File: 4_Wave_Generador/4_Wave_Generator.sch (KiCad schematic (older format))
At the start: 119 parts, among them J1 RS232, J10 Jumper, J11 Jumper, J12 Jumper, J13 Jumper, J14 Jumper, J15 Jumper, J2 I2C, J3 RS232_PIC, J4 RESET, J5 Jumper, J7 Jumper, P1 ECG INPUTS, P10 INPUT_ADC_PIC, P11 PWM_MUX1, P12 RG_8421, P13 CON_MUX2, P14 OUTPUT_TARJET, P15 OUTPUT_DIG_PIC, P16 OUTPUT_DIG_ATMEGA328P, P2 PIC_PROGRAMER, P3 SPI, P4 AD8232_CONTROL, P5 ENTRADA_OXIMETRO, P6 CONN_01X04, P7 CONN_01X04, P8 MCLK_EXTERNAL, P9 SPI_AD9833, SW1 SW_Push, SW2 RESET_PIC, U1 PIC16F688, U2 AD8232_A, U3 ATMEGA328P-AU_MIO, U4 AD9833, U5 LD1117S33TR_MIO, U6 ADG819, U7 ADG819, U8 AD8421, Y1 Crystal_8MHz, Y2 XRCHA_16M

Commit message: GENERADOR_V8
ORGANIZACION DE ELEMENTOS
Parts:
- removed P5: ENTRADA_OXIMETRO, symbol CONN_02X03
- removed R17: 1K, Resistors_SMD:R_0805_HandSoldering, symbol 1K
- added JP5: PASO_A/D, Pin_Headers:Pin_Header_Straight_1x02_Pitch2.54mm, symbol PASO_A/D
- added P5: OXIMETRO, Foot_Prints_Manager_Outputs:OXIMETRO, symbol CONN_01X03
- added P?: 5V, Foot_Prints_Manager_Outputs:SUPPLY_5V, symbol CONN_01X04
- added R17: 20K, Resistors_SMD:R_0805_HandSoldering, symbol 20K
- JP4: value AREF -> J_AREF
- P10: footprint (none) -> Foot_Prints_Manager_Outputs:ADC_PIC
- P11: value PWM_MUX1 -> IN_MUX1; footprint (none) -> Foot_Prints_Manager_Outputs:IN_MUX1
- P12: footprint (none) -> Foot_Prints_Manager_Outputs:RG_8421
- P13: value CON_MUX2 -> IN_MUX2; footprint (none) -> Foot_Prints_Manager_Outputs:IN_MUX2
- P14: footprint (none) -> Foot_Prints_Manager_Outputs:VOUT
- P15: footprint (none) -> Pin_Headers:Pin_Header_Straight_1x04_Pitch2.54mm
- P16: footprint (none) -> Foot_Prints_Manager_Outputs:OUTPUT_ATMEGA
- P2: footprint Pin_Headers:Pin_Header_Angled_1x05_Pitch2.54mm -> Foot_Prints_Manager_Outputs:PIC_PROGRAMER
- P3: value SPI -> SPI_MICRO
- P6: value CONN_01X04 -> SUPPLY -12; footprint Pin_Headers:Pin_Header_Angled_1x04_Pitch2.54mm -> Foot_Prints_Manager_Outputs:SUPPLY_-12V
- P7: value CONN_01X04 -> SUPPLY +12; footprint Pin_Headers:Pin_Header_Angled_1x04_Pitch2.54mm -> Foot_Prints_Manager_Outputs:SUPPLY_12V
- P8: footprint Pin_Headers:Pin_Header_Angled_1x04_Pitch2.54mm -> Foot_Prints_Manager_Outputs:MCLK_EXTERNAL
- P9: footprint (none) -> Foot_Prints_Manager_Outputs:SPI_AD9833
- W1, W10, W11, W12, W2, W3, W4, W5, W6, W7, W8, W9: footprint (none) -> Measurement_Points:Measurement_Point_Round-TH_Small
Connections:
- net labels added: OXIMETRO, RG_PIN2, RG_PIN3
- net labels removed: A_AD5270_1, OXI_1, OXI_2, OXI_3, W_AD5270_1
- wire segments 343 -> 345
- no-connect marks 6 -> 8
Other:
- note added: "MICROCONTROLLER \nATMEGA 328P"
- note removed: "MICROCONTROLADOR \nATMEGA 328P"
- moved on the sheet: C10, D1, D3, D5, D7, P6, P7, R2, R22, R23, R24

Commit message: GENERADOR_V9
DISTRIBUCION DE COMPONENTES
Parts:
- removed C13: 0.1uF, Capacitors_SMD:C_0805_HandSoldering, symbol 0.1uF
- removed J1: RS232, Foot_Prints_Manager_Outputs:RS232, symbol CONN_01X03
- removed J2: I2C, Foot_Prints_Manager_Outputs:I2C_2X4, symbol CONN_01X02
- removed J3: RS232_PIC, Foot_Prints_Manager_Outputs:RS232, symbol CONN_01X03
- removed P11: IN_MUX1, Foot_Prints_Manager_Outputs:IN_MUX1, symbol CONN_01X02
- removed P15: OUTPUT_DIG_PIC, Pin_Headers:Pin_Header_Straight_1x04_Pitch2.54mm, symbol CONN_01X04
- removed P16: OUTPUT_DIG_ATMEGA328P, Foot_Prints_Manager_Outputs:OUTPUT_ATMEGA, symbol CONN_01X12
- removed P6: SUPPLY -12, Foot_Prints_Manager_Outputs:SUPPLY_-12V, symbol CONN_01X04
- removed P7: SUPPLY +12, Foot_Prints_Manager_Outputs:SUPPLY_12V, symbol CONN_01X04
- removed P?: 5V, Foot_Prints_Manager_Outputs:SUPPLY_5V, symbol CONN_01X04
- added C9: 0.1uF, Capacitors_SMD:C_0805_HandSoldering, symbol 0.1uF
- added J6, J8: Jumper, Pin_Headers:Pin_Header_Straight_1x02_Pitch2.54mm, symbol Jumper-RESCUE-PCB_OSCILLATOR
- added JP6: MIN_SANGRADO, Pin_Headers:Pin_Header_Straight_1x03_Pitch2.54mm, symbol JUMPER3
- added P15: MUX_S1, Pin_Headers:Pin_Header_Straight_1x02_Pitch2.54mm, symbol CONN_01X02
- added P16: PD5, Pin_Headers:Pin_Header_Straight_1x01_Pitch2.54mm, symbol CONN_01X01
- added P17: SUPPLY_-12V, Foot_Prints_Manager_Outputs:SUPPLY_-12V, symbol CONN_01X02
- added P18: RS232, Foot_Prints_Manager_Outputs:RS232, symbol CONN_01X03
- added P19: I2C, Foot_Prints_Manager_Outputs:I2C_2X4, symbol CONN_01X02
- added P20: PD6, Pin_Headers:Pin_Header_Straight_1x01_Pitch2.54mm, symbol CONN_01X01
- added P21: PD7, Pin_Headers:Pin_Header_Straight_1x01_Pitch2.54mm, symbol CONN_01X01
- added P22: PB0, Pin_Headers:Pin_Header_Straight_1x01_Pitch2.54mm, symbol CONN_01X01
- added P23: PB1, Pin_Headers:Pin_Header_Straight_1x01_Pitch2.54mm, symbol CONN_01X01
- added P24: PC0, Pin_Headers:Pin_Header_Straight_1x01_Pitch2.54mm, symbol CONN_01X01
- added P25: PC1, Pin_Headers:Pin_Header_Straight_1x01_Pitch2.54mm, symbol CONN_01X01
- added P26: PC2, Pin_Headers:Pin_Header_Straight_1x01_Pitch2.54mm, symbol CONN_01X01
- added P27: PC3, Pin_Headers:Pin_Header_Straight_1x01_Pitch2.54mm, symbol CONN_01X01
- added P28: PD2, Pin_Headers:Pin_Header_Straight_1x01_Pitch2.54mm, symbol CONN_01X01
- added P29: PD3, Pin_Headers:Pin_Header_Straight_1x01_Pitch2.54mm, symbol CONN_01X01
- added P30: PD4, Pin_Headers:Pin_Header_Straight_1x01_Pitch2.54mm, symbol CONN_01X01
- added P31, P32, P33, P34: TORNILLO, Mounting_Holes:MountingHole_3.2mm_M3_Pad_Via, symbol CONN_01X01
- added P35: RS232_PIC, Foot_Prints_Manager_Outputs:RS232, symbol CONN_01X03
- added P6: SUPPLY_12V, Foot_Prints_Manager_Outputs:SUPPLY_12V, symbol CONN_01X02
- added P7: SUPPLY_VDD, Foot_Prints_Manager_Outputs:SUPPLY_5V, symbol CONN_01X02
- added U9: ADG819, Housings_SSOP:MSOP-8_3x3mm_Pitch0.65mm, symbol ADG819
- P13: value IN_MUX2 -> OUTPUT_DIG_PIC; footprint Foot_Prints_Manager_Outputs:IN_MUX2 -> Pin_Headers:Pin_Header_Straight_1x02_Pitch2.54mm
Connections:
- net labels added: MODULATED, PWM, PWM_ATMEGA, SELECTOR
- net labels removed: PD5, PD6, PD7, SDN_OFF
- no-connect marks 8 -> 15
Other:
- note added: "MULTIPLEXER_3\n"
- note removed: "MUX_1\n"
- note removed: "MUX_2"
- moved on the sheet: C14, C15, C16, C17, C20, C21, C22, C23, C24, C25, C26, C28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

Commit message: GENERADOR_V10
RUTEADO MICRO
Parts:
- removed P16: PD5, Pin_Headers:Pin_Header_Straight_1x01_Pitch2.54mm, symbol CONN_01X01
- removed P20: PD6, Pin_Headers:Pin_Header_Straight_1x01_Pitch2.54mm, symbol CONN_01X01
- removed P21: PD7, Pin_Headers:Pin_Header_Straight_1x01_Pitch2.54mm, symbol CONN_01X01
- removed P22: PB0, Pin_Headers:Pin_Header_Straight_1x01_Pitch2.54mm, symbol CONN_01X01
- removed P23: PB1, Pin_Headers:Pin_Header_Straight_1x01_Pitch2.54mm, symbol CONN_01X01
- removed P24: PC0, Pin_Headers:Pin_Header_Straight_1x01_Pitch2.54mm, symbol CONN_01X01
- removed P25: PC1, Pin_Headers:Pin_Header_Straight_1x01_Pitch2.54mm, symbol CONN_01X01
- removed P26: PC2, Pin_Headers:Pin_Header_Straight_1x01_Pitch2.54mm, symbol CONN_01X01
- removed P27: PC3, Pin_Headers:Pin_Header_Straight_1x01_Pitch2.54mm, symbol CONN_01X01
- removed P28: PD2, Pin_Headers:Pin_Header_Straight_1x01_Pitch2.54mm, symbol CONN_01X01
- removed P29: PD3, Pin_Headers:Pin_Header_Straight_1x01_Pitch2.54mm, symbol CONN_01X01
- removed P30: PD4, Pin_Headers:Pin_Header_Straight_1x01_Pitch2.54mm, symbol CONN_01X01
- added P11: DIG_ATMEGA, Pin_Headers:Pin_Header_Straight_1x04_Pitch2.54mm, symbol CONN_01X04
- added P16: DIG_MICRO, Pin_Headers:Pin_Header_Straight_1x03_Pitch2.54mm, symbol CONN_01X03
- added P20: DIG_ATMEGA2, Pin_Headers:Pin_Header_Straight_1x03_Pitch2.54mm, symbol CONN_01X03
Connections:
- net MODULATING_WAVE is gone; now on net SELECTOR: U3.10 ((PCINT22/OC0A/AIN0)PD6)
- net PB0: now also P20.2 (P2)
- net PB1: now also P20.3 (P3)
- net PC0: now also P11.1 (P1)
- net PC1: now also P11.2 (P2)
- net PC2: now also P11.3 (P3)
- net PC3: now also P11.4 (P4)
- net PD2: now also P16.1 (P1)
- net PD3: now also P16.2 (P2)
- net PD4: now also P16.3 (P3)
- net SELECTOR: no longer U3.11 ((PCINT23/AIN1)PD7)
- new net PD7: P20.1 (P1), U3.11 ((PCINT23/AIN1)PD7)
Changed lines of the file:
@@
 Text Label 6170 2350 0    60   ~ 0
 PD3
-Text Label 8090 10870 1    60   ~ 0
+Text Label 8260 10860 1    60   ~ 0
 PC3
-Text Label 7790 10870 1    60   ~ 0
+Text Label 7960 10860 1    60   ~ 0
 PC0
-Text Label 7890 10870 1    60   ~ 0
+Text Label 8060 10860 1    60   ~ 0
 PC1
-Text Label 7990 10870 1    60   ~ 0
+Text Label 8160 10860 1    60   ~ 0
 PC2
-Text Label 7490 10870 1    60   ~ 0
-SELECTOR
 Text Notes 6010 1080 0    60   ~ 0
 MICROCONTROLLER \nATMEGA 328P
-Text Label 8290 10870 1    60   ~ 0
+Text Label 7150 10850 1    60   ~ 0
 PD3
-Text Label 8190 10870 1    60   ~ 0
+Text Label 7050 10850 1    60   ~ 0
 PD2
 Text Label 5610 2090 0    60   ~ 0
@@
 	7690 10100 7690 10870
 Wire Wire Line
-	7790 10100 7790 10870
-Wire Wire Line
-	7890 10100 7890 10870
-Wire Wire Line
-	7990 10100 7990 10870
-Wire Wire Line
-	7290 10100 7290 10870
-Wire Wire Line
-	7390 10100 7390 10870
+	7960 10090 7960 10860
+Wire Wire Line
+	8060 10090 8060 10860
+Wire Wire Line
+	8160 10090 8160 10860
 Wire Wire Line
 	7490 10100 7490 10870
@@
 	7590 10100 7590 10870
 Wire Wire Line
-	8090 10100 8090 10870
-Wire Wire Line
-	8290 10100 8290 10870
-Wire Wire Line
-	8390 10100 8390 10870
+	8260 10090 8260 10860
+Wire Wire Line
+	7150 10080 7150 10850
+Wire Wire Line
+	7250 10080 7250 10850
 Wire Notes Line
 	640  7890 4960 7890
@@
 OUTPUT GAVE GENERATOR
 Wire Wire Line
-	8190 10100 8190 10870
-Text Label 8390 10870 1    60   ~ 0
+	7050 10080 7050 10850
+Text Label 7250 10850 1    60   ~ 0
 PD4
 Text Label 6650 10870 1    60   ~ 0
@@
 P 6700 9900
 F 0 "P13" H 6700 10050 50  0000 C CNN
-F 1 "OUTPUT_DIG_PIC" V 6810 9830 50  0000 C CNN
+F 1 "OUTPUT_DIG_PIC" V 6820 9900 50  0000 C CNN
 F 2 "Pin_Headers:Pin_Header_Straight_1x02_Pitch2.54mm" H 6700 9900 50  0001 C CNN
 F 3 "" H 6700 9900 50  0000 C CNN
@@
 	0    -1   -1   0
 $EndComp
-Text Label 7390 10870 1    60   ~ 0
-MODULATING_WAVE
 Text Label 13340 5850 0    60   ~ 0
 BASE_WAVE
@@
 Text Label 11130 9130 0    60   ~ 0
 PWM_ATMEGA
-Text Label 7290 10870 1    60   ~ 0
-PWM_ATMEGA
 Wire Notes Line
 	9740 9500 9740 7920
@@
 Wire Notes Line
 	12740 7920 12740 9500
+Text Label 9240 1790 2    60   ~ 0
+PD7
 Text Label 9240 1700 2    60   ~ 0
-MODULATING_WAVE
-Text Label 9240 1790 2    60   ~ 0
 SELECTOR
 $Comp
@@
 	0    -1   -1   0
 $EndComp
-$Comp
-L CONN_01X01 P20
-U 1 1 59D7476C
-P 7390 9900
-F 0 "P20" V 7310 9910 50  0000 C CNN
-F 1 "PD6" H 7510 9900 50  0000 C CNN
-F 2 "Pin_Headers:Pin_Header_Straight_1x01_Pitch2.54mm" H 7390 9900 50  0001 C CNN
-F 3 "" H 7390 9900 50  0000 C CNN
-	1    7390 9900
-	0    -1   -1   0
-$EndComp
-$Comp
-L CONN_01X01 P21
-U 1 1 59D74A09
-P 7490 9900
-F 0 "P21" V 7410 9910 50  0000 C CNN
-F 1 "PD7" H 7610 9900 50  0000 C CNN
-F 2 "Pin_Headers:Pin_Header_Straight_1x01_Pitch2.54mm" H 7490 9900 50  0001 C CNN
-F 3 "" H 7490 9900 50  0000 C CNN
-	1    7490 9900
-	0    -1   -1   0
-$EndComp
-$Comp
-L CONN_01X01 P22
-U 1 1 59D7CC91
-P 7590 9900
-F 0 "P22" V 7510 9910 50  0000 C CNN
-F 1 "PB0" H 7710 9900 50  0000 C CNN
-F 2 "Pin_Headers:Pin_Header_Straight_1x01_Pitch2.54mm" H 7590 9900 50  0001 C CNN
-F 3 "" H 7590 9900 50  0000 C CNN
-	1    7590 9900
-	0    -1   -1   0
-$EndComp
-$Comp
-L CONN_01X01 P23
-U 1 1 59D7CC97
-P 7690 9900
-F 0 "P23" V 7610 9910 50  0000 C CNN
-F 1 "PB1" H 7810 9900 50  0000 C CNN
-F 2 "Pin_Headers:Pin_Header_Straight_1x01_Pitch2.54mm" H 7690 9900 50  0001 C CNN
-F 3 "" H 7690 9900 50  0000 C CNN
-	1    7690 9900
-	0    -1   -1   0
-$EndComp
-$Comp
-L CONN_01X01 P24
-U 1 1 59D7CC9D
-P 7790 9900
-F 0 "P24" V 7710 9910 50  0000 C CNN
-F 1 "PC0" H 7910 9900 50  0000 C CNN
-F 2 "Pin_Headers:Pin_Header_Straight_1x01_Pitch2.54mm" H 7790 9900 50  0001 C CNN
-F 3 "" H 7790 9900 50  0000 C CNN
-	1    7790 9900
-	0    -1   -1   0
-$EndComp
-$Comp
-L CONN_01X01 P25
-U 1 1 59D88535
-P 7890 9900
-F 0 "P25" V 7810 9910 50  0000 C CNN
-F 1 "PC1" H 8010 9900 50  0000 C CNN
-F 2 "Pin_Headers:Pin_Header_Straight_1x01_Pitch2.54mm" H 7890 9900 50  0001 C CNN
-F 3 "" H 7890 9900 50  0000 C CNN
-	1    7890 9900
-	0    -1   -1   0
-$EndComp
-$Comp
-L CONN_01X01 P26
-U 1 1 59D8853B
-P 7990 9900
-F 0 "P26" V 7910 9910 50  0000 C CNN
-F 1 "PC2" H 8110 9900 50  0000 C CNN
-F 2 "Pin_Headers:Pin_Header_Straight_1x01_Pitch2.54mm" H 7990 9900 50  0001 C CNN
-F 3 "" H 7990 9900 50  0000 C CNN
-	1    7990 9900
-	0    -1   -1   0
-$EndComp
-$Comp
-L CONN_01X01 P27
-U 1 1 59D88541
-P 8090 9900
-F 0 "P27" V 8010 9910 50  0000 C CNN
-F 1 "PC3" H 8210 9900 50  0000 C CNN
-F 2 "Pin_Headers:Pin_Header_Straight_1x01_Pitch2.54mm" H 8090 9900 50  0001 C CNN
-F 3 "" H 8090 9900 50  0000 C CNN
-	1    8090 9900
-	0    -1   -1   0
-$EndComp
-$Comp
-L CONN_01X01 P28
-U 1 1 59D88547
-P 8190 9900
-F 0 "P28" V 8110 9910 50  0000 C CNN
-F 1 "PD2" H 8310 9900 50  0000 C CNN
-F 2 "Pin_Headers:Pin_Header_Straight_1x01_Pitch2.54mm" H 8190 9900 50  0001 C CNN
-F 3 "" H 8190 9900 50  0000 C CNN
-	1    8190 9900
-	0    -1   -1   0
-$EndComp
-$Comp
-L CONN_01X01 P29
-U 1 1 59D8854D
-P 8290 9900
-F 0 "P29" V 8210 9910 50  0000 C CNN
-F 1 "PD3" H 8410 9900 50  0000 C CNN
-F 2 "Pin_Headers:Pin_Header_Straight_1x01_Pitch2.54mm" H 8290 9900 50  0001 C CNN
-F 3 "" H 8290 9900 50  0000 C CNN
-	1    8290 9900
-	0    -1   -1   0
-$EndComp
-$Comp
-L CONN_01X01 P30
-U 1 1 59D88553
-P 8390 9900
-F 0 "P30" V 8310 9910 50  0000 C CNN
-F 1 "PD4" H 8510 9900 50  0000 C CNN
-F 2 "Pin_Headers:Pin_Header_Straight_1x01_Pitch2.54mm" H 8390 9900 50  0001 C CNN
-F 3 "" H 8390 9900 50  0000 C CNN
-	1    8390 9900
-	0    -1   -1   0
-$EndComp
 Text Label 8940 3150 2    60   ~ 0
 PC3
@@
 Wire Notes Line
 	5320 7360 5320 6790
-$Comp
-L CONN_01X01 P16
-U 1 1 59D6AAB0
-P 7290 9900
-F 0 "P16" V 7210 9910 50  0000 C CNN
-F 1 "PD5" H 7410 9900 50  0000 C CNN
-F 2 "Pin_Headers:Pin_Header_Straight_1x01_Pitch2.54mm" H 7290 9900 50  0001 C CNN
-F 3 "" H 7290 9900 50  0000 C CNN
-	1    7290 9900
-	0    -1   -1   0
-$EndComp
 $Comp
 L CONN_01X03 P35
@@
 Text Label 9240 1890 2    60   ~ 0
 PB0
+Text Label 7490 10870 1    60   ~ 0
+PD7
+$Comp
+L CONN_01X04 P11
+U 1 1 59D8C525
+P 8110 9890
+F 0 "P11" H 8110 10140 50  0000 C CNN
+F 1 "DIG_ATMEGA" V 8210 9890 50  0000 C CNN
+F 2 "Pin_Headers:Pin_Header_Straight_1x04_Pitch2.54mm" H 8110 9890 50  0001 C CNN
+F 3 "" H 8110 9890 50  0000 C CNN
+	1    8110 9890
+	0    -1   -1   0
+$EndComp
+$Comp
+L CONN_01X03 P16
+U 1 1 59D926A2
+P 7150 9880
+F 0 "P16" H 7150 10080 50  0000 C CNN
+F 1 "DIG_MICRO" V 7250 9880 50  0000 C CNN
+F 2 "Pin_Headers:Pin_Header_Straight_1x03_Pitch2.54mm" H 7150 9880 50  0001 C CNN
+F 3 "" H 7150 9880 50  0000 C CNN
+	1    7150 9880
+	0    -1   -1   0
+$EndComp
+$Comp
+L CONN_01X03 P20
+U 1 1 59D97200
+P 7590 9900
+F 0 "P20" H 7590 10100 50  0000 C CNN
+F 1 "DIG_ATMEGA2" V 7690 9900 50  0000 C CNN
+F 2 "Pin_Headers:Pin_Header_Straight_1x03_Pitch2.54mm" H 7590 9900 50  0001 C CNN
+F 3 "" H 7590 9900 50  0000 C CNN
+	1    7590 9900
+	0    -1   -1   0
+$EndComp
 $EndSCHEMATC

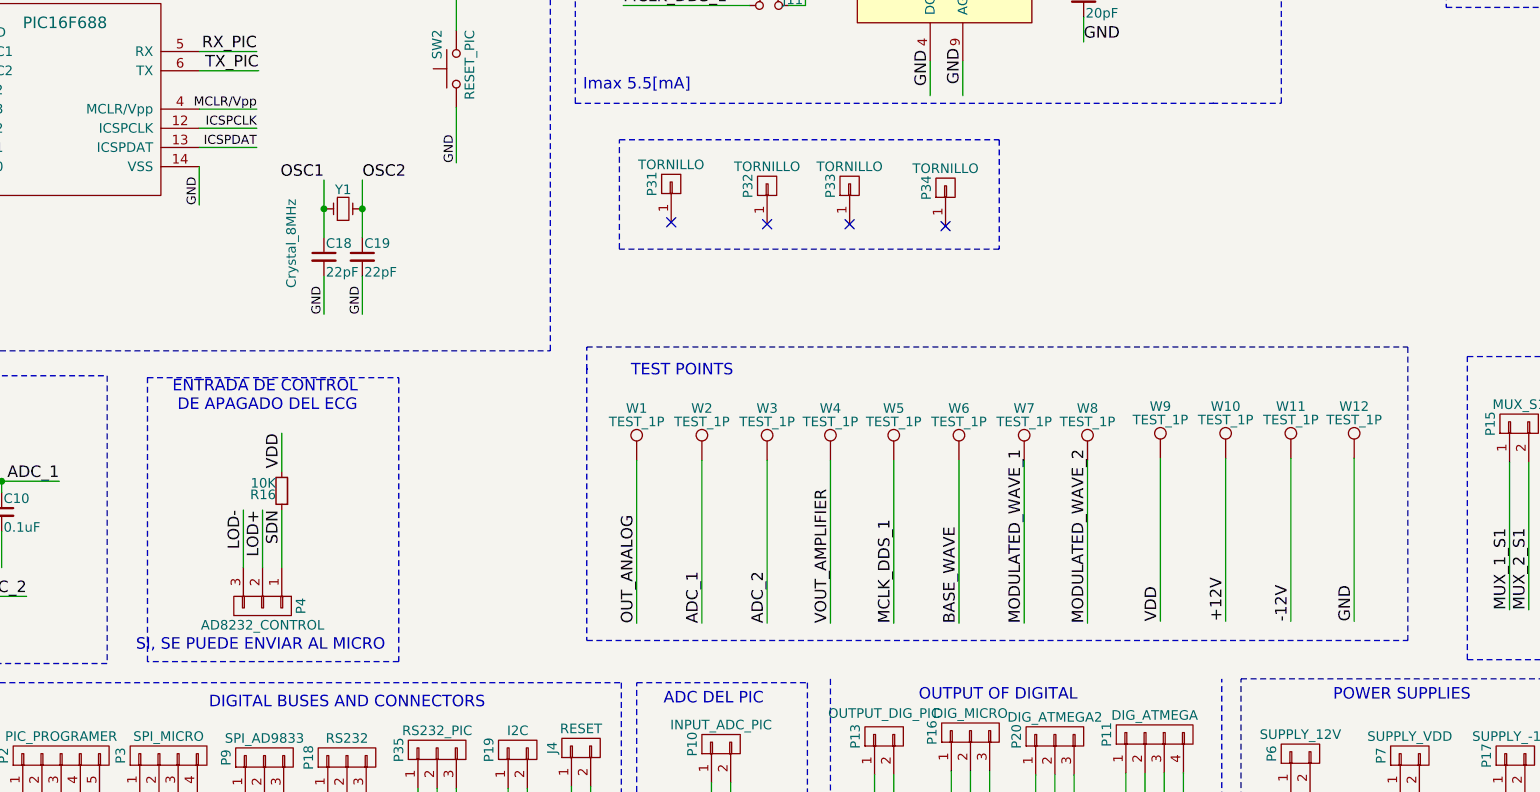
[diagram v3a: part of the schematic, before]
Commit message: GENERADOR_V11
NUEVAS CONEXIONES
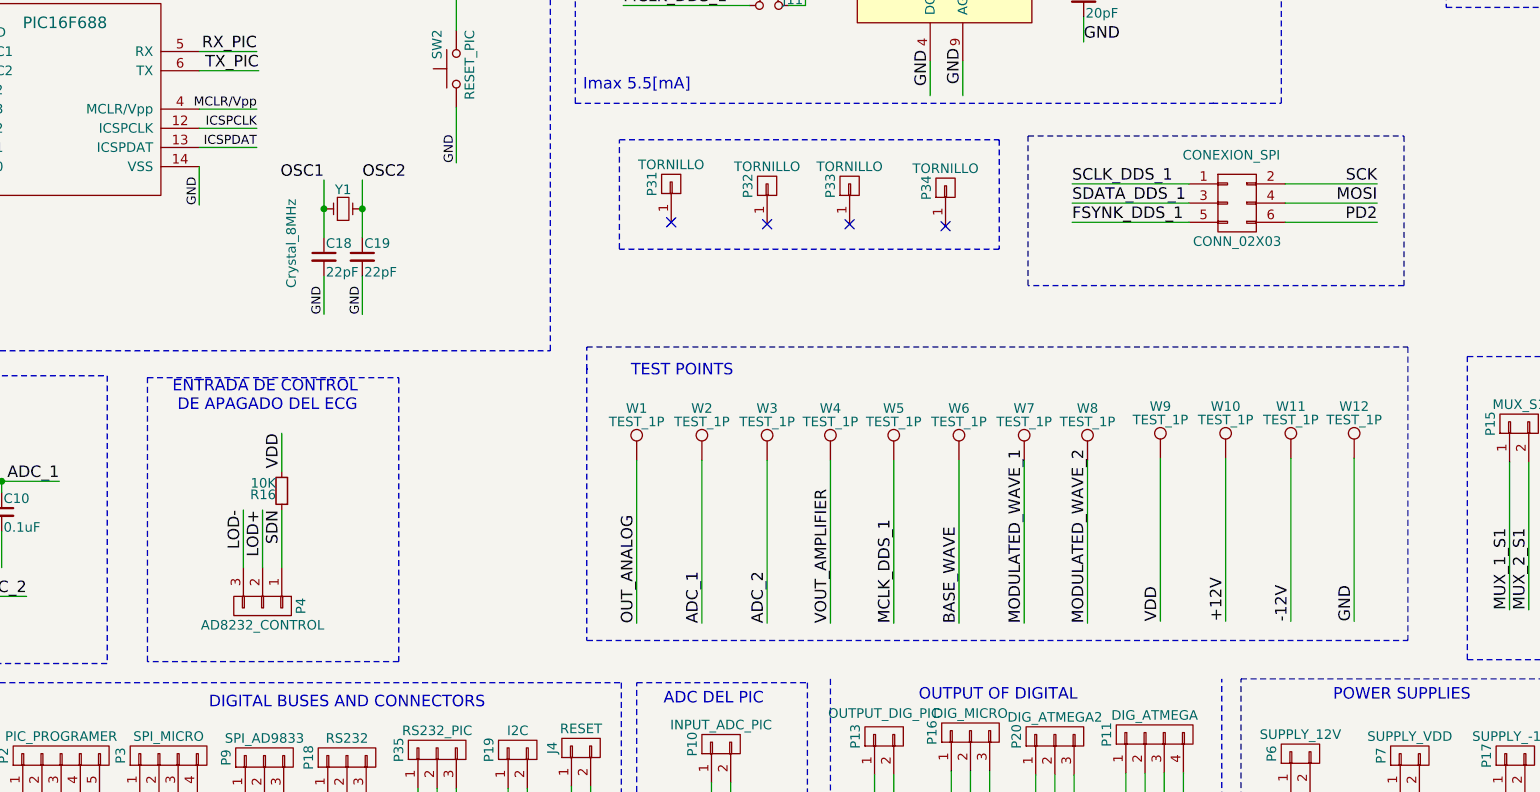
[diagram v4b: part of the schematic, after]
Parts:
- added CONEXION_SPI: CONN_02X03, Pin_Headers:Pin_Header_Straight_2x03_Pitch2.54mm, symbol CONN_02X03
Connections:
- net FSYNK_DDS_1: now also CONEXION_SPI.5 (P5)
- net MOSI: now also CONEXION_SPI.4 (P4)
- net PD2: now also CONEXION_SPI.6 (P6)
- net SCK: now also CONEXION_SPI.2 (P2)
- net SCLK_DDS_1: now also CONEXION_SPI.1 (P1)
- net SDATA_DDS_1: now also CONEXION_SPI.3 (P3)
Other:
- note removed: "SI, SE PUEDE ENVIAR AL MICRO"
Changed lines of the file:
@@
 Text Label 3560 8320 3    60   ~ 0
 VDD
-Text Notes 2800 9460 0    60   ~ 0
-SI, SE PUEDE ENVIAR AL MICRO
 Text Label 10380 10110 0    47   ~ 0
 OUT_ANALOG
@@
 	0    -1   -1   0
 $EndComp
+$Comp
+L CONN_02X03 CONEXION_SPI
+U 1 1 59D69BA8
+P 8540 7120
+F 0 "CONEXION_SPI" H 8510 7370 50  0000 C CNN
+F 1 "CONN_02X03" H 8540 6920 50  0000 C CNN
+F 2 "Pin_Headers:Pin_Header_Straight_2x03_Pitch2.54mm" H 8540 5920 50  0001 C CNN
+F 3 "" H 8540 5920 50  0000 C CNN
+	1    8540 7120
+	1    0    0    -1
+$EndComp
+Text Label 7680 7020 0    60   ~ 0
+SCLK_DDS_1
+Text Label 7680 7120 0    60   ~ 0
+SDATA_DDS_1
+Text Label 7680 7220 0    60   ~ 0
+FSYNK_DDS_1
+Wire Wire Line
+	7680 7020 8290 7020
+Wire Wire Line
+	7680 7120 8290 7120
+Wire Wire Line
+	7680 7220 8290 7220
+Wire Wire Line
+	8790 7020 9270 7020
+Wire Wire Line
+	8790 7120 9270 7120
+Wire Wire Line
+	8790 7220 9270 7220
+Text Label 9270 7120 2    60   ~ 0
+MOSI
+Text Label 9270 7020 2    60   ~ 0
+SCK
+Text Label 9270 7220 2    60   ~ 0
+PD2
+Wire Notes Line
+	7450 6770 9410 6770
+Wire Notes Line
+	9410 6770 9410 7550
+Wire Notes Line
+	9410 7550 7450 7550
+Wire Notes Line
+	7450 7550 7450 6770
 $EndSCHEMATC
